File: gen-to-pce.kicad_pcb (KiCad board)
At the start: 2 copper layers, 69.8 x 31.8 mm, 11 parts, among them J1 DB9 (M), J2 M-DIN-8 (F), U1 74HC04, U2 74HC74, U3 74HC157

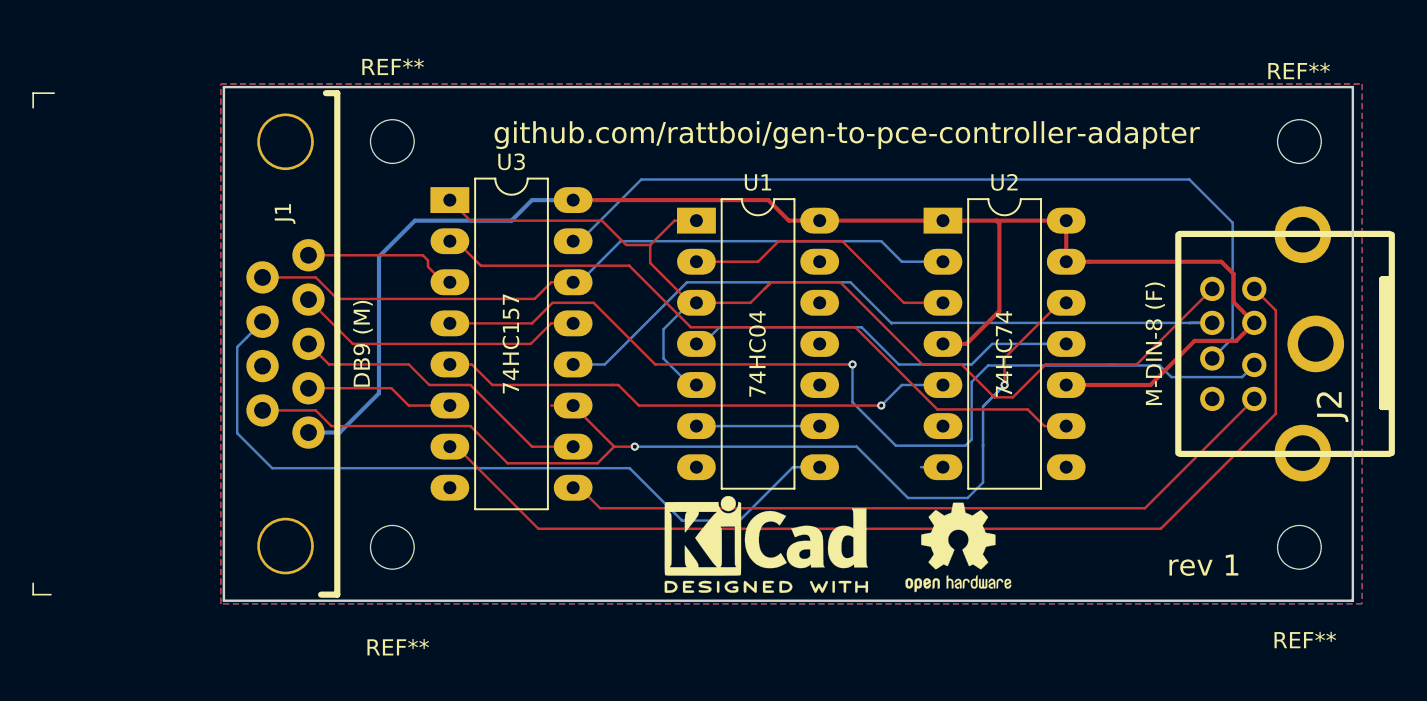
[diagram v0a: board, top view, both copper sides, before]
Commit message: Add DPDT switch, reroute to account for switch
The switch swaps the A button and Start button, which makes it the same
as an Avenue Pad 3, basically. With the Avenue Pad 3, the extra button
exists where the A button is on the Genesis, and the mapping is selected
by a switch on the controller. Some games use III mapped to Sel, some
use III mapped to Run.

The original design had A (which you can consider III) hard-mapped to
Sel. Now it is selectable, which increases compatibility with games that
mapped III to Run instead.
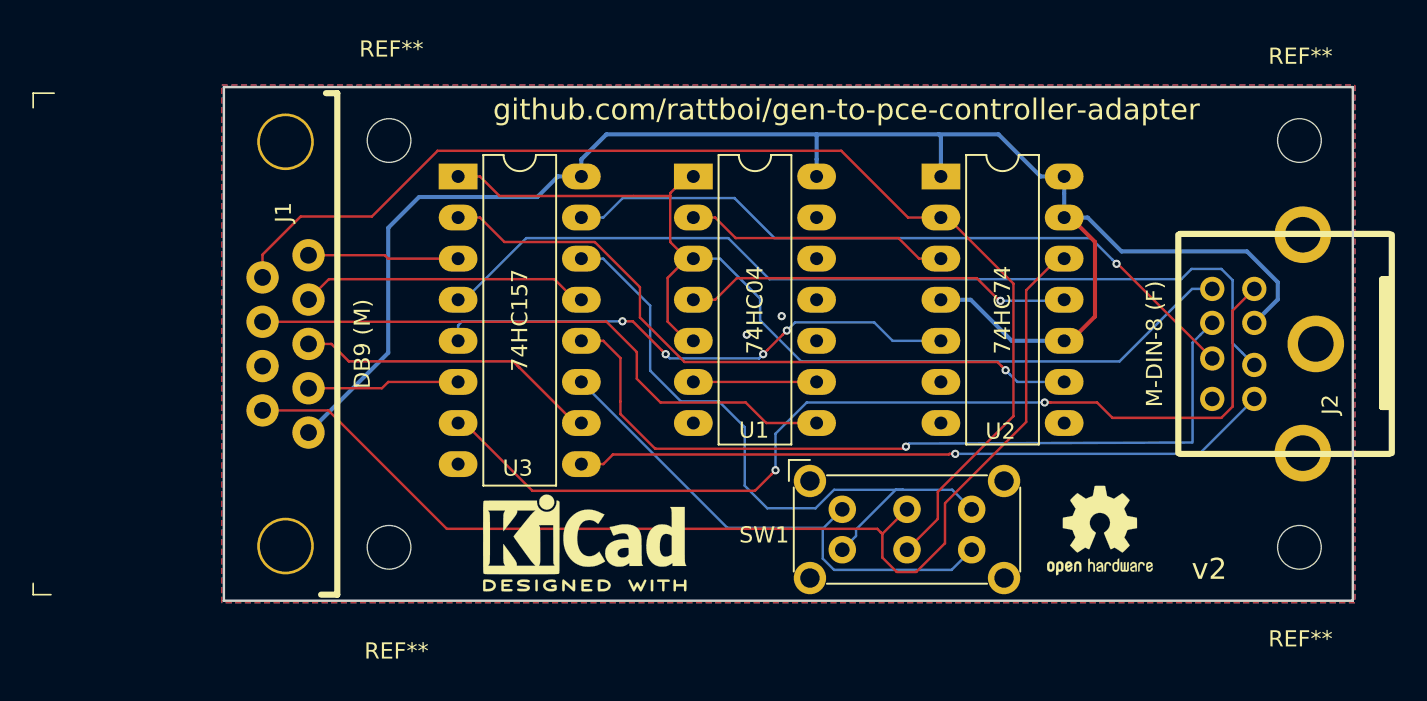
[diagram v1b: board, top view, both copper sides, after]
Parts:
- removed the REF** at (108.2, 100.3)
- removed the REF** at (108.3, 74.8)
- removed the REF** at (164.2, 75.1)
- added REF**: MountingHole_2.7mm_M2.5, MountingHole:MountingHole_2.7mm_M2.5, F.Cu at (108.0, 100.2)
- added REF**: MountingHole_2.7mm_M2.5, MountingHole:MountingHole_2.7mm_M2.5, F.Cu at (108.0, 75.1)
- added REF**: MountingHole_2.7mm_M2.5, MountingHole:MountingHole_2.7mm_M2.5, F.Cu at (164.3, 75.1)
- added SW1: SW_DPDT_x2, Button_Switch_THT:SW_E-Switch_EG2219_DPDT_Angled, F.Cu at (136.0, 97.9)
- moved REF** 11.2 mm to (120.1, 99.9)
- moved REF** 8.81 mm to (151.9, 99.2)
- moved U1 2.74 mm to (126.8, 77.3)
- moved U2 2.73 mm to (142.1, 77.3)
- moved U3 1.55 mm to (112.3, 77.3)
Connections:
- U3 pad 11: Net-(J1-Pad9) -> Net-(SW1-Pad1)
- U3 pad 14: Net-(J1-Pad6) -> Net-(SW1-Pad3)
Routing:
- net Net-(SW1-Pad3): track 0.00 -> 41.5 mm
- net Net-(SW1-Pad1): track 0.00 -> 32.2 mm
- net Net-(J1-Pad6): track 45.0 -> 73.1 mm
- net Net-(J1-Pad7): track 47.2 -> 37.8 mm
- net Net-(J2-Pad7): track 52.4 -> 43.6 mm, vias 0 -> 1
- net Net-(J2-Pad4): track 44.5 -> 50.5 mm, vias 0 -> 1
- net Net-(J2-Pad6): track 69.9 -> 64.2 mm
- net Net-(J2-Pad2): track 60.2 -> 56.9 mm, vias 1 -> 0
- net Net-(J2-Pad3): track 64.4 -> 61.7 mm, vias 0 -> 2
- net Net-(J1-Pad9): track 68.4 -> 70.9 mm, vias 2 -> 0
- net GND: track 2.55 -> 0.00 mm, vias 0 -> 2
- net Net-(J2-Pad5): track 45.4 -> 43.3 mm, vias 0 -> 1
- net Net-(U1-Pad4): track 26.1 -> 24.1 mm, vias 0 -> 1
- net +5V: track 102.9 -> 104.7 mm
- net Net-(U1-Pad2): track 17.7 -> 16.4 mm
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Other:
- board text added: "v2"
- board text removed: "rev 1"

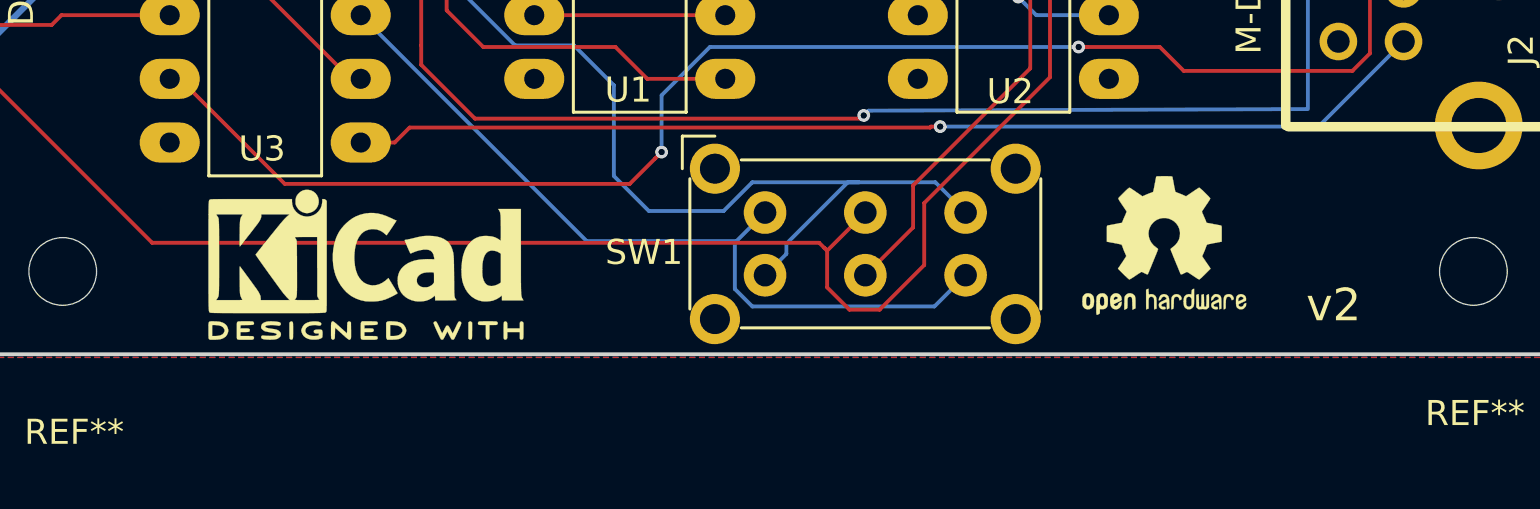
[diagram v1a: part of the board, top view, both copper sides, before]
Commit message: Add III button (A on genesis) mapping to silkscreen
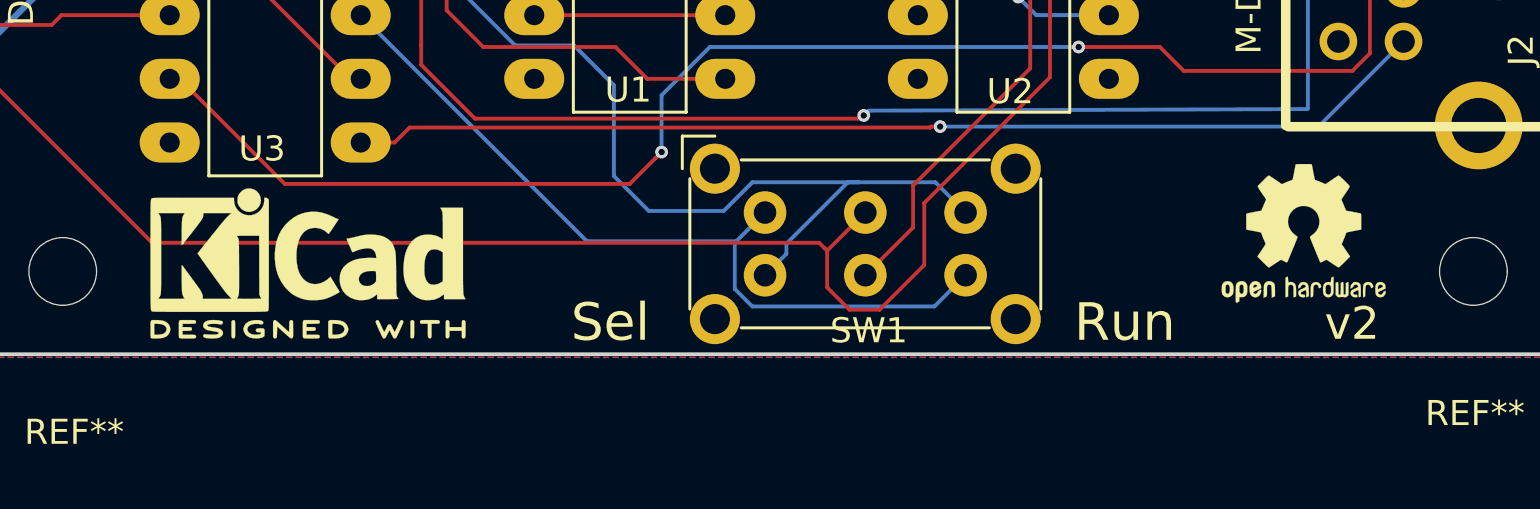
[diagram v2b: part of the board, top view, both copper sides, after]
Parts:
- moved REF** 5.58 mm to (157.5, 98.7)
- moved REF** 2.31 mm to (117.8, 99.9)
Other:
- board text added: "Run"
- board text added: "Sel"
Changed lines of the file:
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@@
   (general
     (thickness 1.6)
-    (drawings 13)
+    (drawings 15)
     (tracks 242)
     (zones 0)
@@
     (descr "E-Switch slide switch, EG series, DPDT, right angle, http://spec_sheets.e-switch.com/specs/P040170.pdf")
     (tags "switch DPDT")
-    (fp_text reference SW1 (at -4.826 1.5875) (layer F.SilkS)
+    (fp_text reference SW1 (at 4.1402 4.7117) (layer F.SilkS)
       (effects (font (size 1 1) (thickness 0.15)))
     )
@@
   )
   (module Symbol:KiCad-Logo2_6mm_SilkScreen (layer F.Cu)
-    (at 120.0912 99.9236)
+    (at 117.7798 99.8728)
     (descr "KiCad Logo")
     (tags "Logo KiCad")
@@
   )
   (module Symbol:OSHW-Logo2_7.3x6mm_SilkScreen (layer F.Cu)
-    (at 151.9428 99.1616)
+    (at 157.5054 98.679)
     (descr "Open Source Hardware Symbol")
     (tags "Logo Symbol OSHW")
@@
       (xy -2.549664 1.91989) (xy -2.469928 1.911165) (xy -2.400256 1.919918)) (layer F.SilkS) (width 0.01))
   )
-  (gr_text v2 (at 158.6992 101.5492) (layer F.SilkS)
+  (gr_text Run (at 150.368 102.235) (layer F.SilkS)
+    (effects (font (size 1.5 1.5) (thickness 0.3)))
+  )
+  (gr_text Sel (at 129.8448 102.235) (layer F.SilkS)
+    (effects (font (size 1.5 1.5) (thickness 0.3)))
+  )
+  (gr_text v2 (at 159.4358 102.2858) (layer F.SilkS)
     (effects (font (size 1.3 1.3) (thickness 0.2)))
   )
